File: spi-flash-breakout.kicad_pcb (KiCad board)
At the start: 2 copper layers, 30 x 30 mm, 14 parts, among them J1 Prog, J2 Test Left, J3 Test Right, U1 MX25U12835FM2I-10G

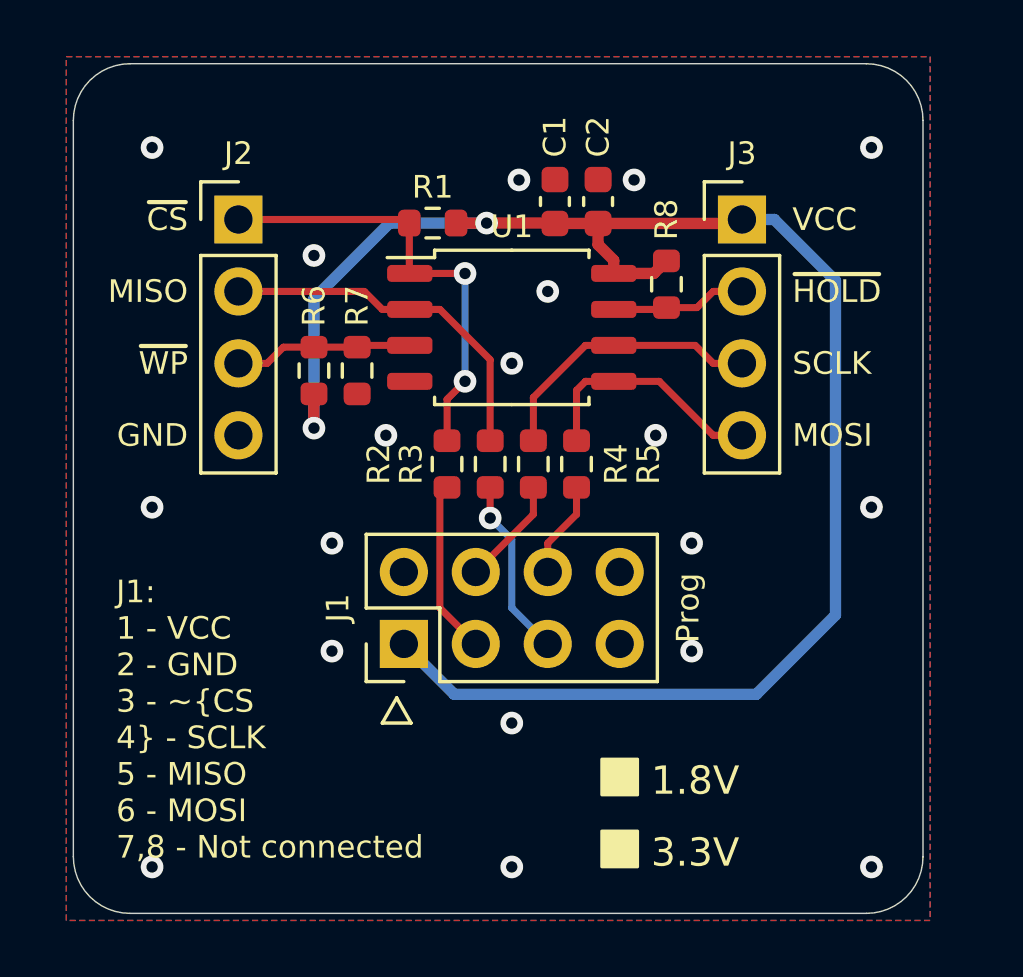
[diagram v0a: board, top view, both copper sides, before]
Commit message: Project upgrade to KiCad 6
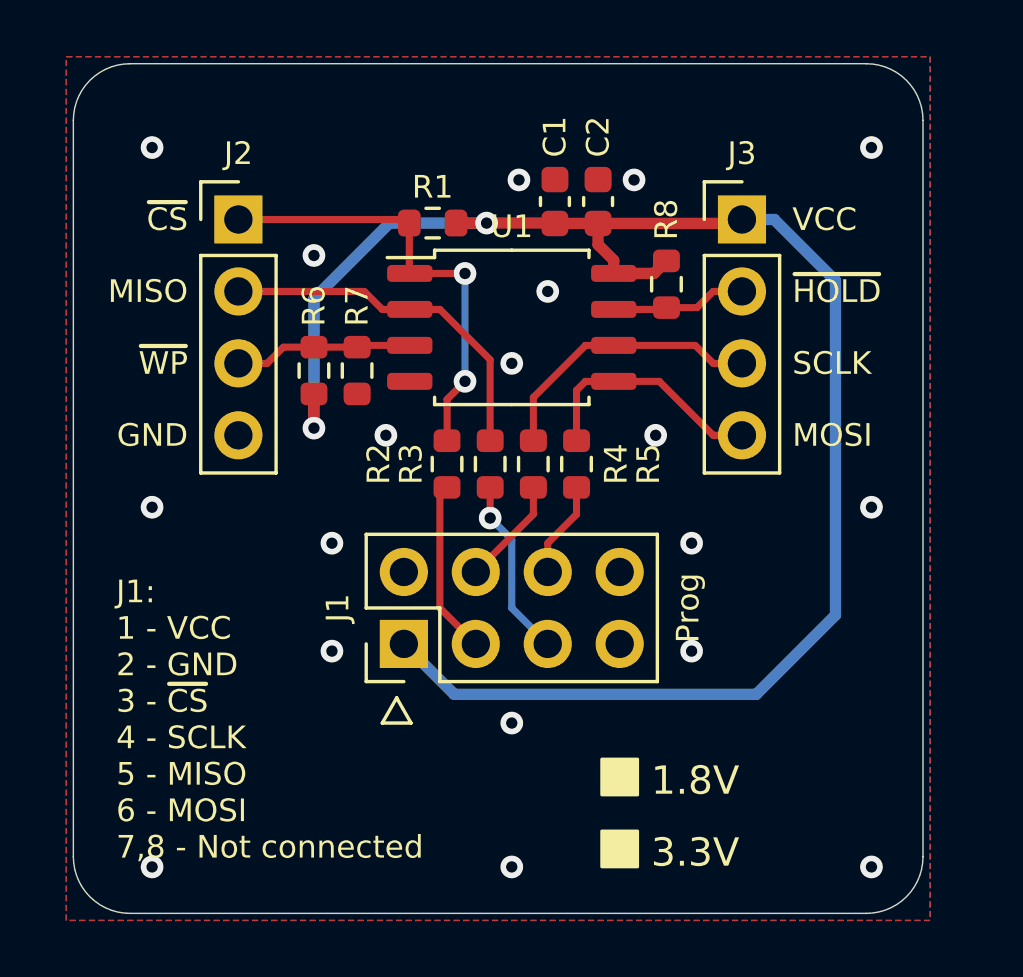
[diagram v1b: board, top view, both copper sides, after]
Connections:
- net /~CS renamed /~{CS}
- net /~HOLD renamed /~{HOLD}
- net /~WP renamed /~{WP}
- J1 pad 7: Net-(J1-Pad7) -> unconnected-(J1-Pad7)
- J1 pad 8: Net-(J1-Pad8) -> unconnected-(J1-Pad8)
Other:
- net class Default removed
- net class Power removed
- board text added: "J1: 1 - VCC 2 - GND 3 - ~{CS} 4 - SCLK 5 - MISO 6 - MOSI 7,8 - Not connected"
- board text added: "~{CS}"
- board text added: "~{HOLD}"
- board text added: "~{WP}"
- board text removed: "J1: 1 - VCC 2 - GND 3 - ~CS 4 - SCLK 5 - MISO 6 - MOSI 7,8 - Not connected"
- board text removed: "~CS"
- board text removed: "~HOLD"
- board text removed: "~WP"
